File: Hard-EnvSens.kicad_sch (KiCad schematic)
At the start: 94 parts, among them J1 TYPE-C-31-M-12, J2 Conn_01x04_Socket, J3 Conn_02x02_Odd_Even, J4 Conn_01x04_Pin, J5 Conn_02x02_Odd_Even, J6 Conn_01x02_Pin, J7 Conn_01x04_Pin, Q1 SS8050, Q2 SS8050, SW1 SW_Push, SW2 SW_Push, SW3 SW_Push, U1 LD1117S33TR_SOT223, U10 BMI160, U11 TPS22918TDBVRQ1, U12 TP4056-42-ESOP8, U13 SPX3819M5-L-3-3, U2 ESP32-C6-WROOM-1, U3 IP5306, U4 VEML7700-TR, U5 DPS368, U6 SGP41-D-R4, U7 SHT40-AD1B-R2, U8 AS7341-DLGT, U9 TPS79318DBVTG4

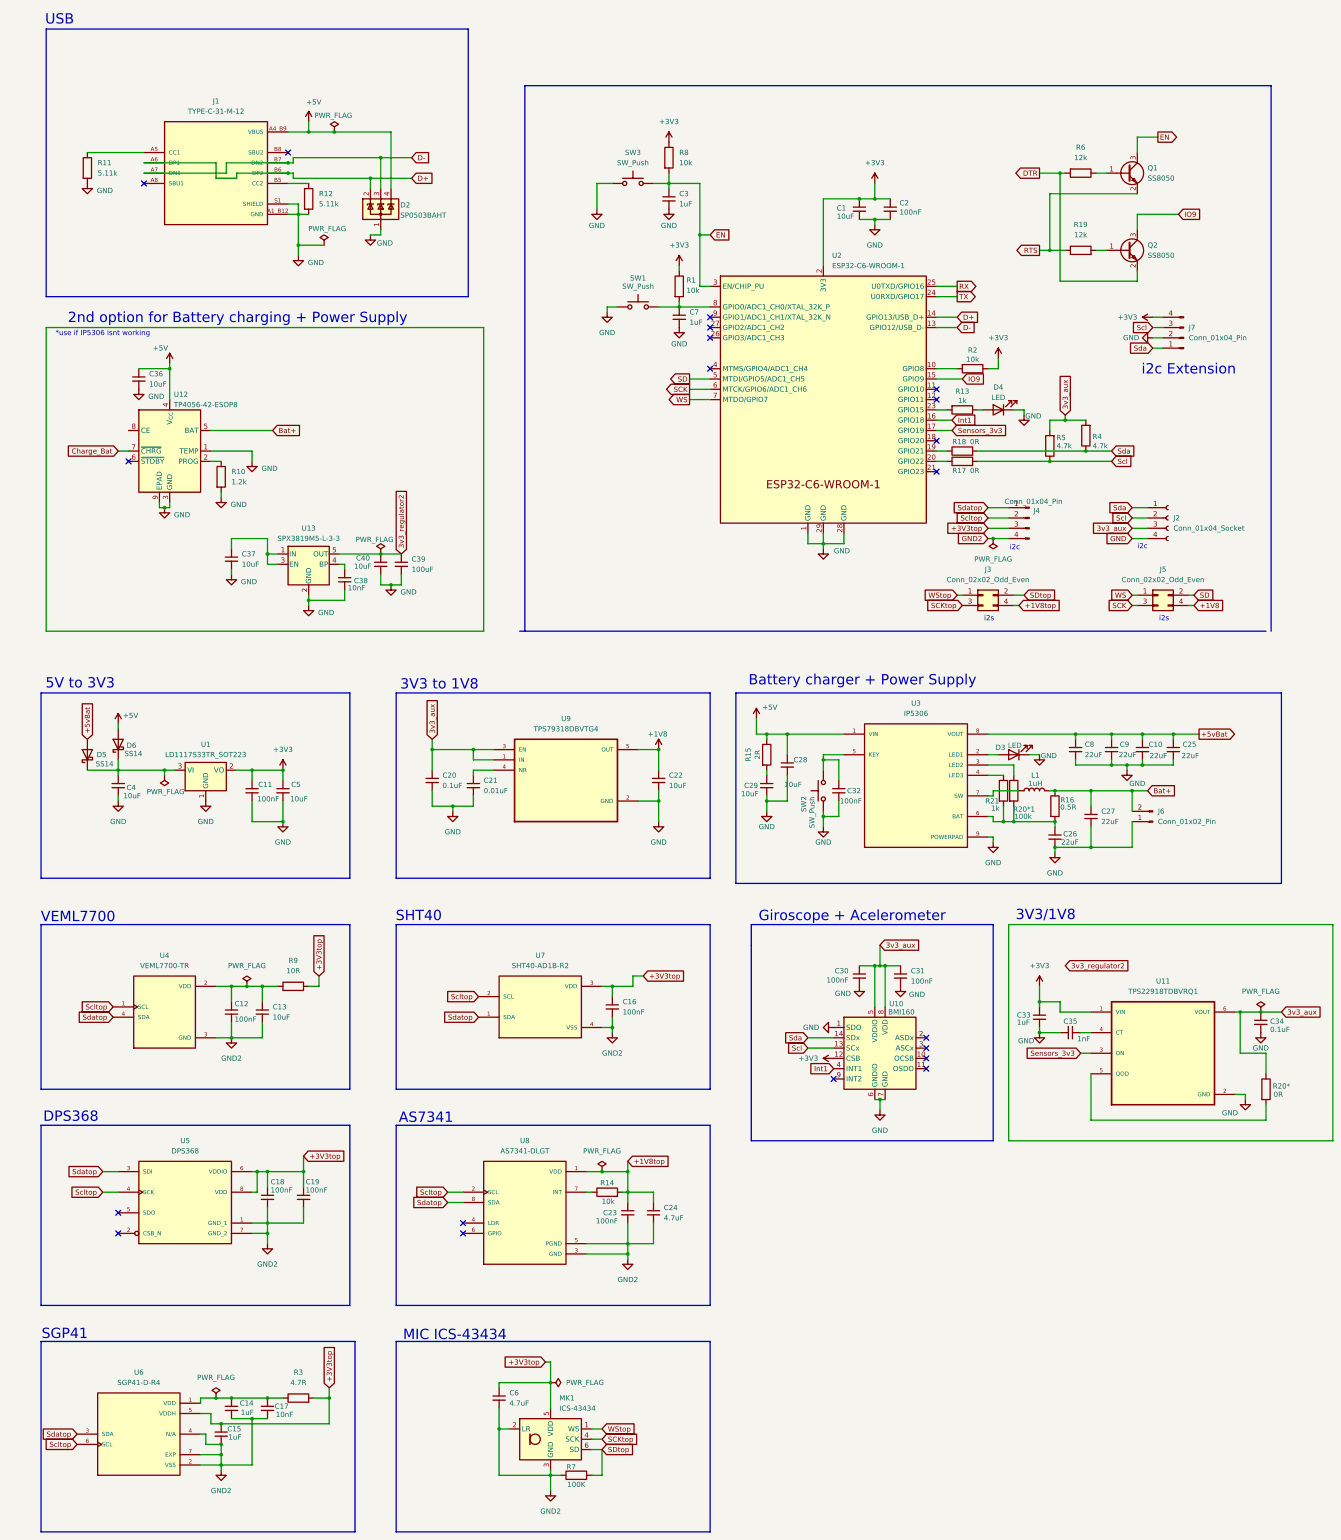
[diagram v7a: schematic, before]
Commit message: small changes + gotta fix the charger
Maybe rotating the charger 2 gets a better pin configuration
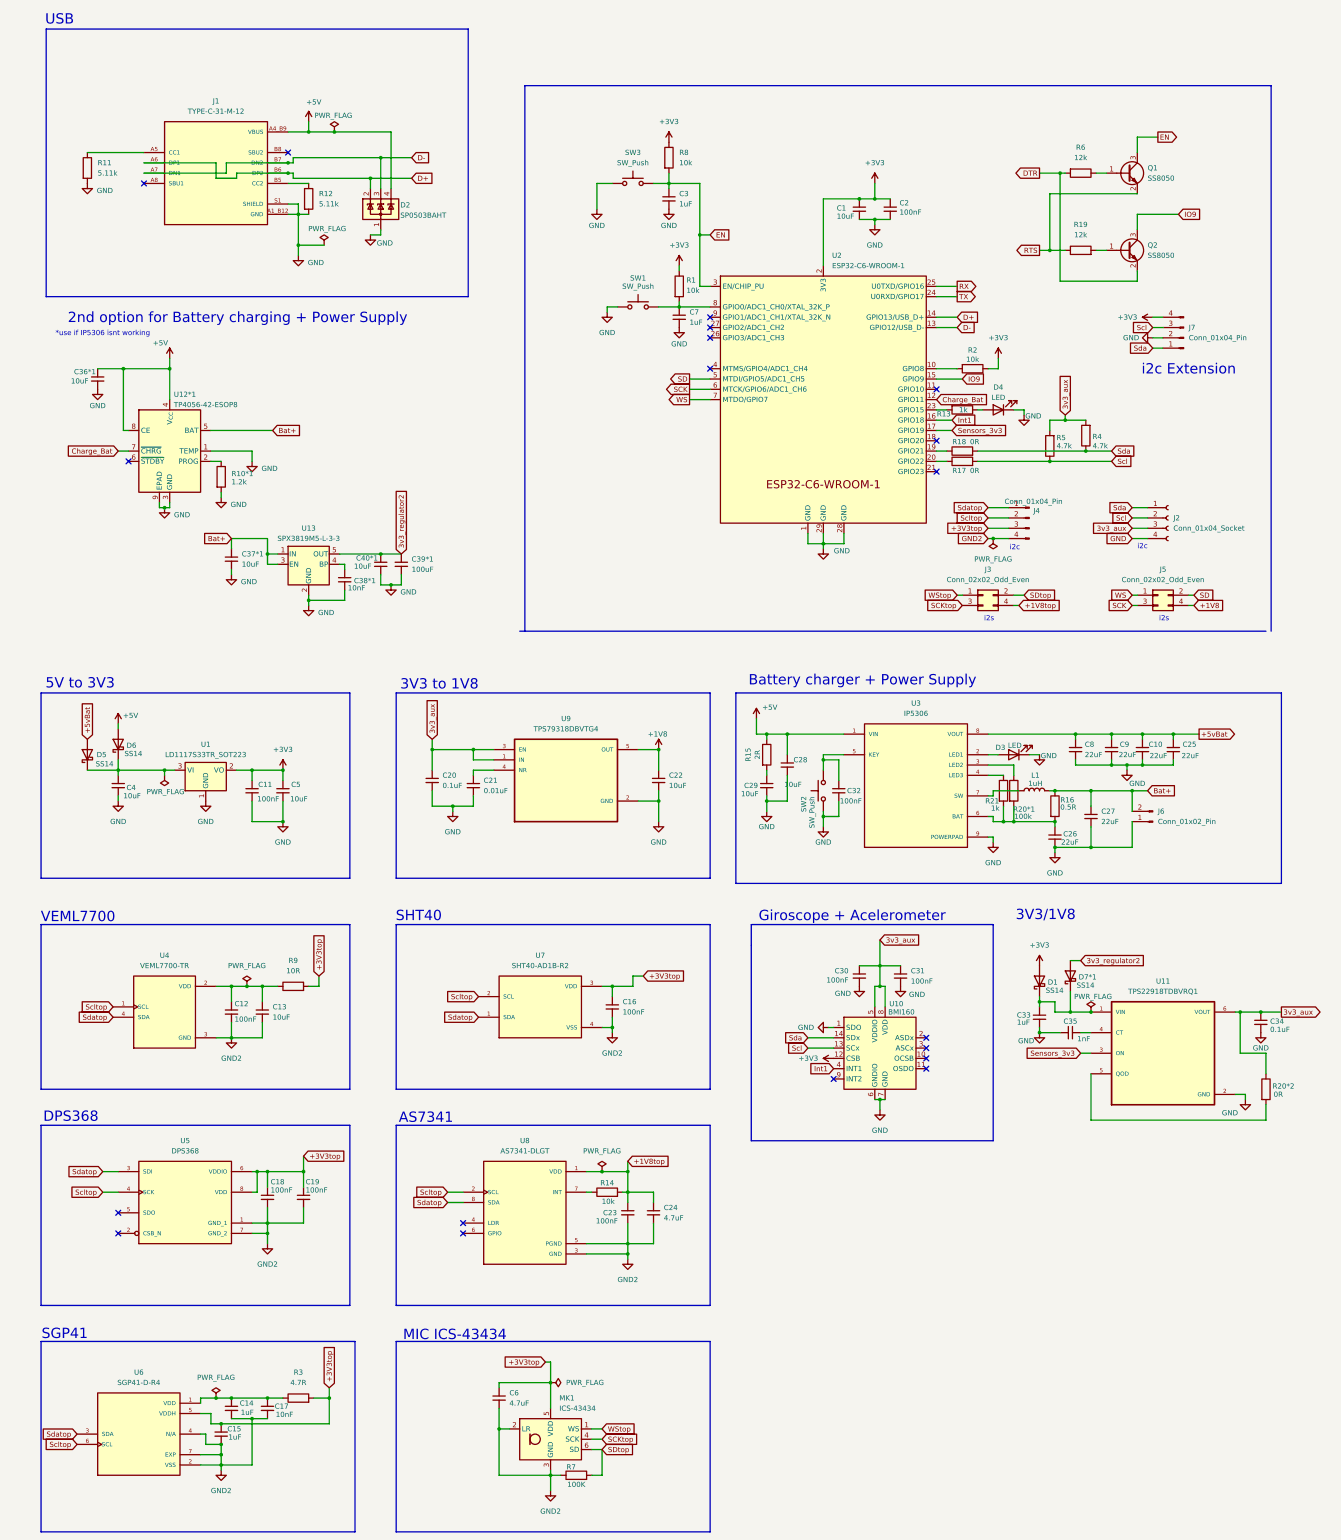
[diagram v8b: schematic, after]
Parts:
- added D1, D7*1: SS14, Diode_SMD:D_SMA, symbol Diode:SS14
- U3: footprint IP5306:SOP127P600X165-9N -> libs:SOP127P600X165-9N
- U5: footprint Biblioteca_Kicad:LGA8S145X65P2X4_200X250X110-V -> libs:LGA8S145X65P2X4_200X250X110-V
- renumbered C36 to C36*1, C37 to C37*1, C38 to C38*1, C39 to C39*1, C40 to C40*1, R10 to R10*1, R20* to R20*2, U12 to U12*1
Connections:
- net +3V3: now also D1.2 (A); no longer C33.1, U11.1 (VIN)
- net +5V: now also U12*1.8 (CE)
- net 3v3_regulator2: now also D7*1.2 (A)
- net Bat+: now also C37*1.1, U13.1 (IN), U13.3 (EN)
- net Charge_Bat: now also U2.12 (GPIO11)
- new net: C33.1, D1.1 (K), D7*1.1 (K), U11.1 (VIN)
- no-connect marks 20 -> 19
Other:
- moved on the sheet: C36*1
